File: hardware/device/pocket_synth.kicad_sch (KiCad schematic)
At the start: 0 parts

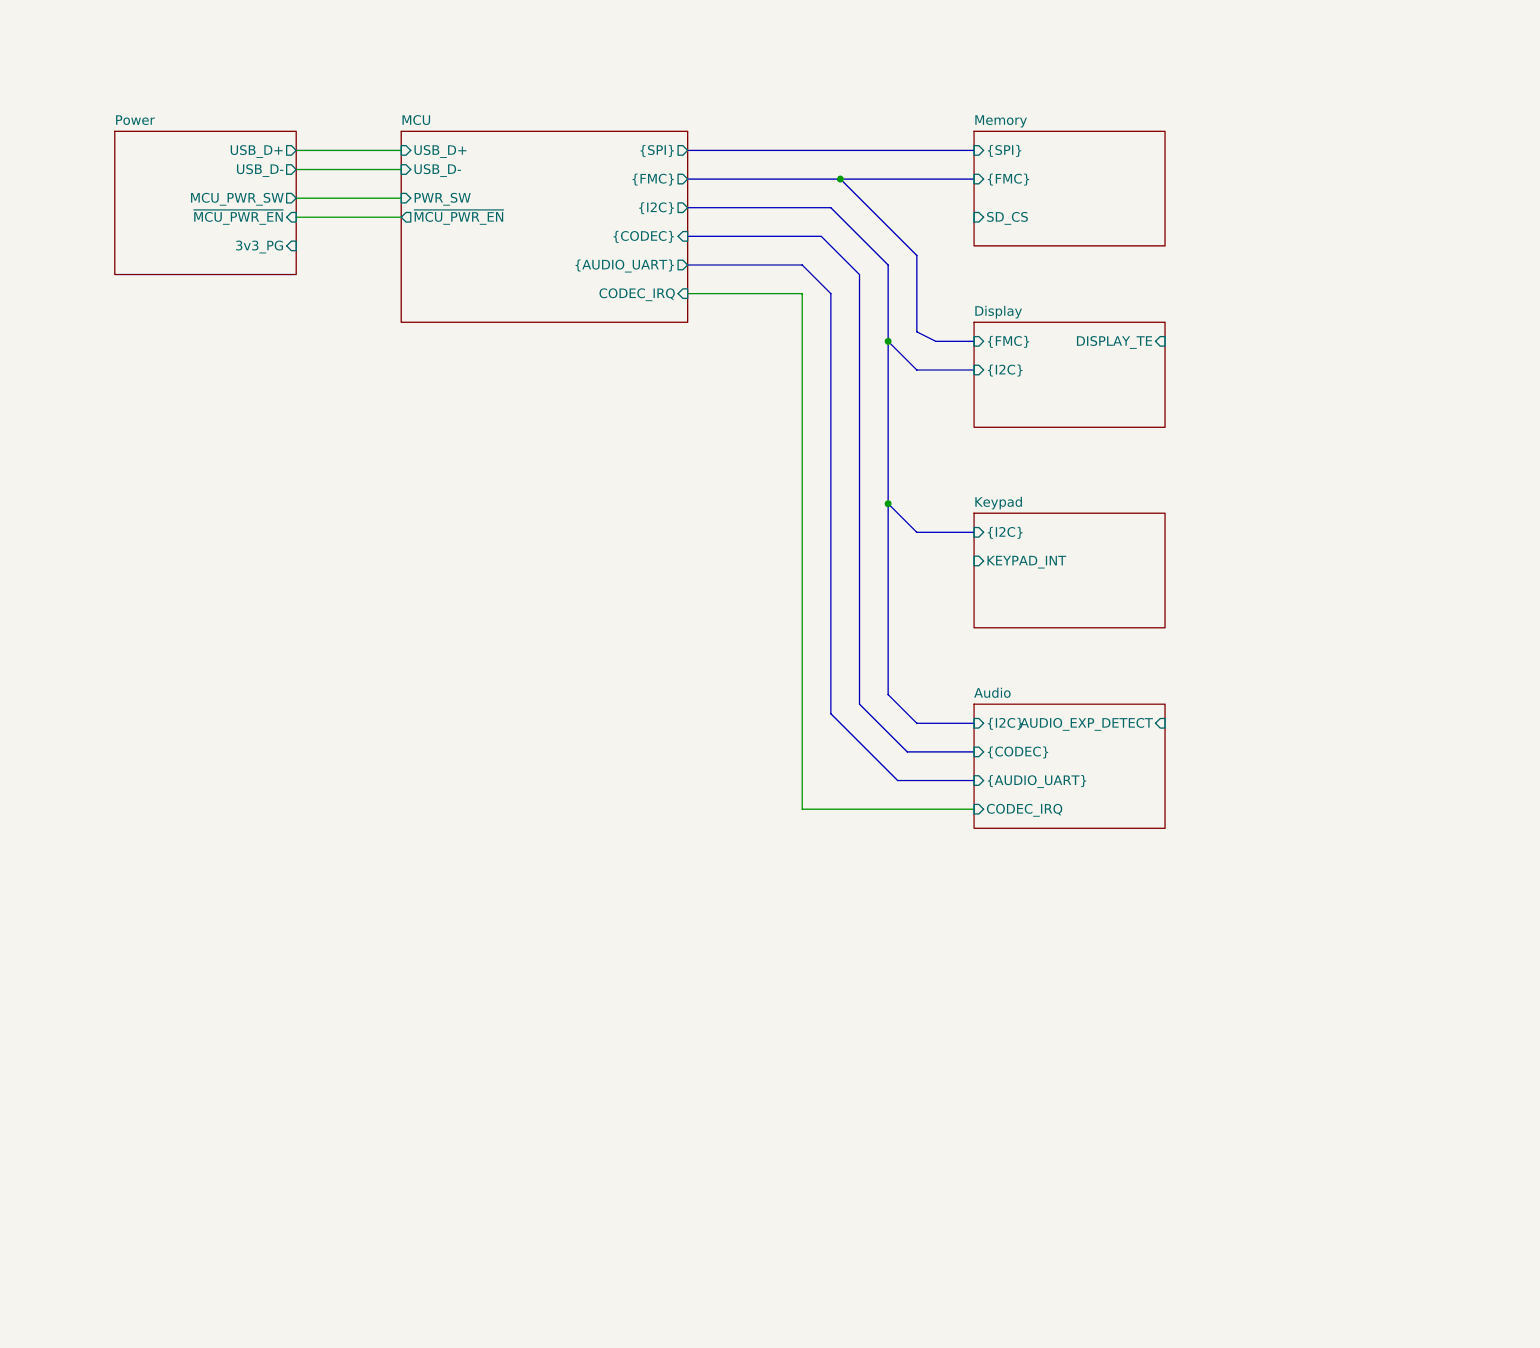
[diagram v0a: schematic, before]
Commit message: feat: various layout, start adding capacitive pads
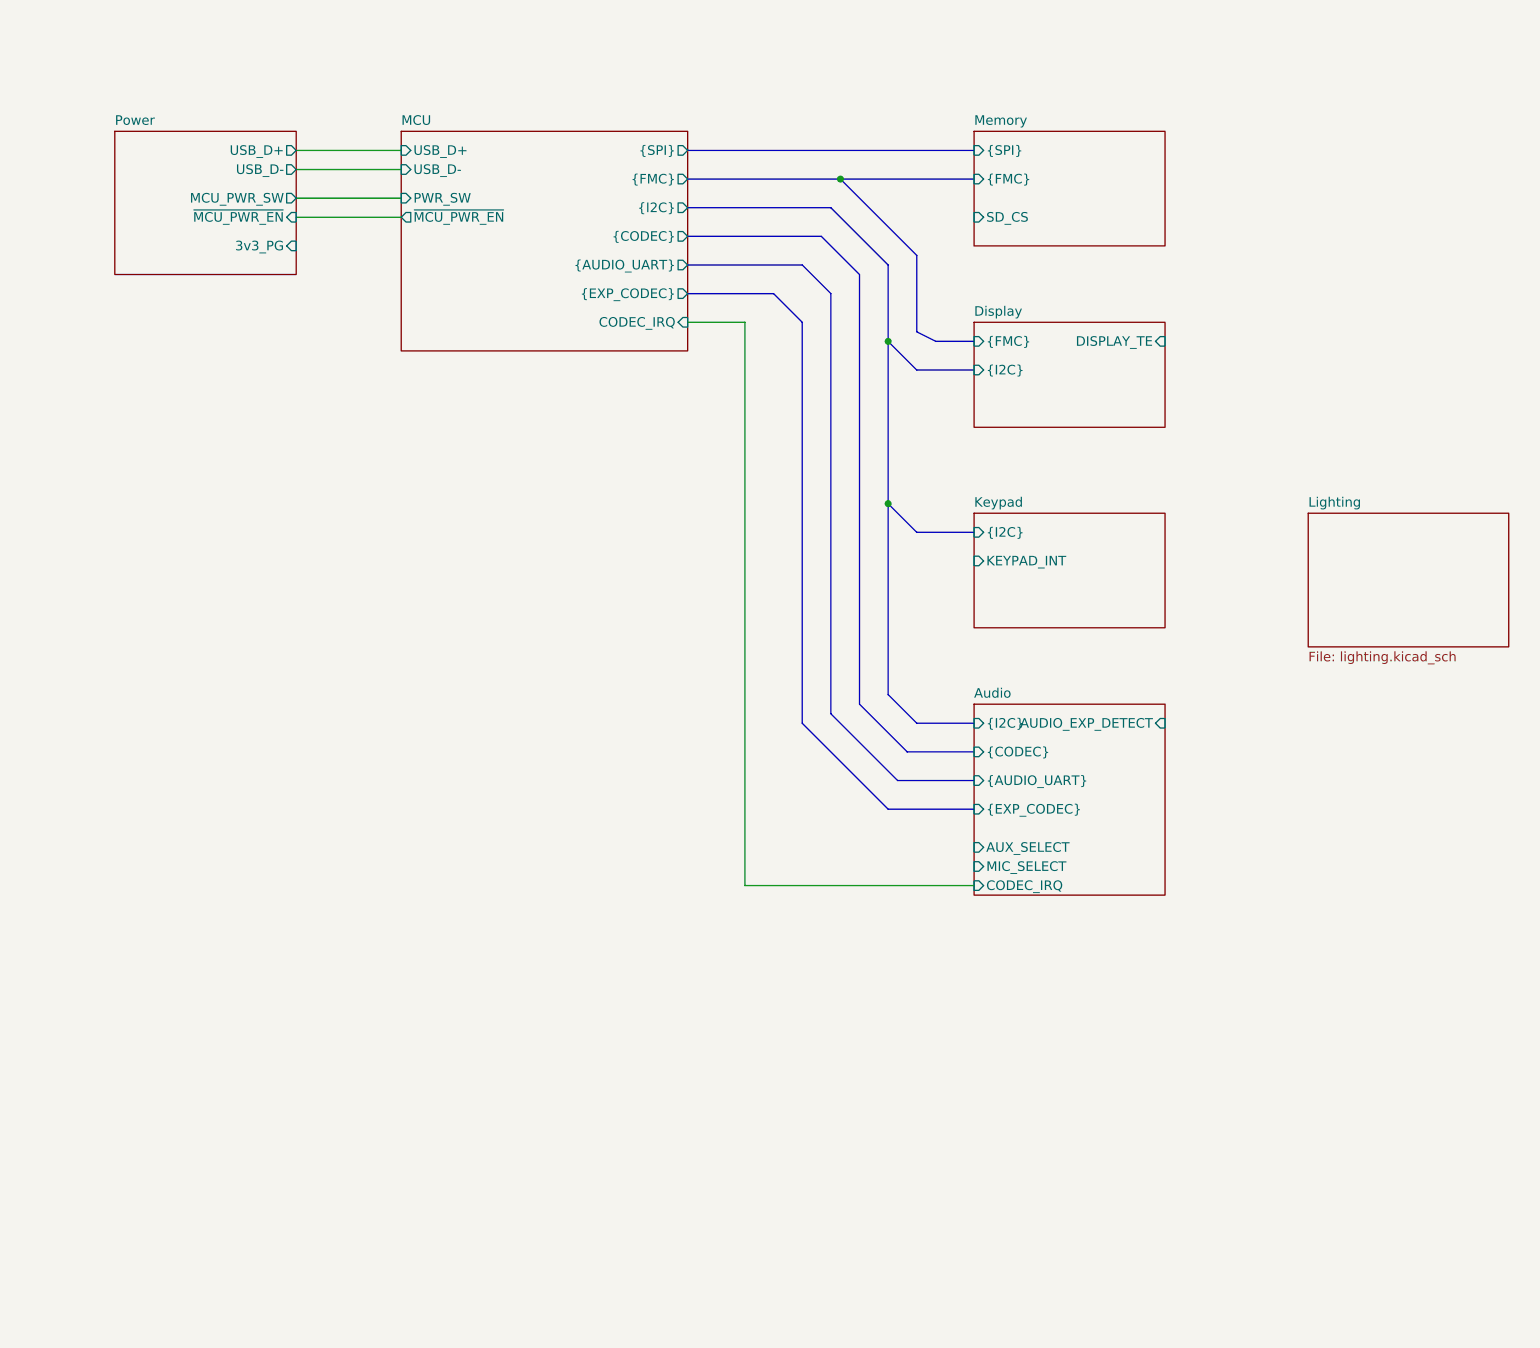
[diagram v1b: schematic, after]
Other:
- added sheet Lighting (lighting.kicad_sch)
- sheet Audio ports: added AUX_SELECT, MIC_SELECT, {EXP_CODEC}; removed none
- sheet MCU ports: added {EXP_CODEC}; removed none
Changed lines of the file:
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@@
 	(wire
 		(pts
-			(xy 116.84 59.69) (xy 116.84 128.27)
+			(xy 109.22 63.5) (xy 109.22 138.43)
+		)
+		(stroke
+			(width 0)
+			(type default)
+		)
+	)
+	(bus
+		(pts
+			(xy 113.03 59.69) (xy 116.84 63.5)
 		)
 		(stroke
@@
 	(wire
 		(pts
-			(xy 101.6 59.69) (xy 116.84 59.69)
+			(xy 101.6 63.5) (xy 109.22 63.5)
+		)
+		(stroke
+			(width 0)
+			(type default)
+		)
+	)
+	(bus
+		(pts
+			(xy 116.84 63.5) (xy 116.84 116.84)
 		)
 		(stroke
@@
 		)
 	)
+	(bus
+		(pts
+			(xy 101.6 59.69) (xy 113.03 59.69)
+		)
+		(stroke
+			(width 0)
+			(type default)
+		)
+	)
 	(wire
 		(pts
-			(xy 116.84 128.27) (xy 139.7 128.27)
+			(xy 109.22 138.43) (xy 139.7 138.43)
 		)
 		(stroke
@@
 	(bus
 		(pts
+			(xy 128.27 128.27) (xy 139.7 128.27)
+		)
+		(stroke
+			(width 0)
+			(type default)
+		)
+	)
+	(bus
+		(pts
 			(xy 120.65 115.57) (xy 129.54 124.46)
 		)
@@
 		(pts
 			(xy 101.6 44.45) (xy 121.92 44.45)
+		)
+		(stroke
+			(width 0)
+			(type default)
+		)
+	)
+	(bus
+		(pts
+			(xy 116.84 116.84) (xy 128.27 128.27)
 		)
 		(stroke
@@
 	(sheet
 		(at 63.5 38.1)
-		(size 38.1 25.4)
+		(size 38.1 29.21)
 		(exclude_from_sim no)
 		(in_bom yes)
@@
 		)
 		(property "Sheetfile" "MCU.kicad_sch"
-			(at 63.5 64.0846 0)
+			(at 63.5 67.8946 0)
 			(effects
 				(font
@@
 			)
 		)
-		(pin "{CODEC}" input
+		(pin "{CODEC}" output
 			(at 101.6 52.07 0)
 			(effects
@@
 		)
 		(pin "CODEC_IRQ" input
-			(at 101.6 59.69 0)
+			(at 101.6 63.5 0)
 			(effects
 				(font
@@
 		(pin "{AUDIO_UART}" output
 			(at 101.6 55.88 0)
+			(effects
+				(font
+					(size 1.27 1.27)
+				)
+				(justify right)
+			)
+		)
+		(pin "{EXP_CODEC}" output
+			(at 101.6 59.69 0)
 			(effects
 				(font
@@
 	(sheet
 		(at 139.7 114.3)
-		(size 25.4 16.51)
+		(size 25.4 25.4)
 		(exclude_from_sim no)
 		(in_bom yes)
@@
 		)
 		(property "Sheetfile" "audio.kicad_sch"
-			(at 139.7 131.3946 0)
+			(at 139.7 140.2846 0)
 			(effects
 				(font
@@
 		)
 		(pin "CODEC_IRQ" input
-			(at 139.7 128.27 180)
+			(at 139.7 138.43 180)
 			(effects
 				(font
@@
 		(pin "{AUDIO_UART}" input
 			(at 139.7 124.46 180)
+			(effects
+				(font
+					(size 1.27 1.27)
+				)
+				(justify left)
+			)
+		)
+		(pin "AUX_SELECT" input
+			(at 139.7 133.35 180)
+			(effects
+				(font
+					(size 1.27 1.27)
+				)
+				(justify left)
+			)
+		)
+		(pin "MIC_SELECT" input
+			(at 139.7 135.89 180)
+			(effects
+				(font
+					(size 1.27 1.27)
+				)
+				(justify left)
+			)
+		)
+		(pin "{EXP_CODEC}" input
+			(at 139.7 128.27 180)
 			(effects
 				(font
@@
 				)
 			)
+		)
+	)
+	(sheet
+		(at 184.15 88.9)
+		(size 26.67 17.78)
+		(exclude_from_sim no)
+		(in_bom yes)
+		(on_board yes)
+		(dnp no)
+		(fields_autoplaced yes)
+		(stroke
+			(width 0.1524)
+			(type solid)
+		)
+		(fill
+			(color 0 0 0 0.0000)
+		)
+		(property "Sheetname" "Lighting"
+			(at 184.15 88.1884 0)
+			(effects
+				(font
+					(size 1.27 1.27)
+				)
+				(justify left bottom)
+			)
+		)
+		(property "Sheetfile" "lighting.kicad_sch"
+			(at 184.15 107.2646 0)
+			(effects
+				(font
+					(size 1.27 1.27)
+				)
+				(justify left top)
+			)
+		)
+		(instances
+			(project "pocket_synth"
+				(path "/485383b8-00f4-4405-b270-de249939cff4"
+					(page "8")
+				)
+			)

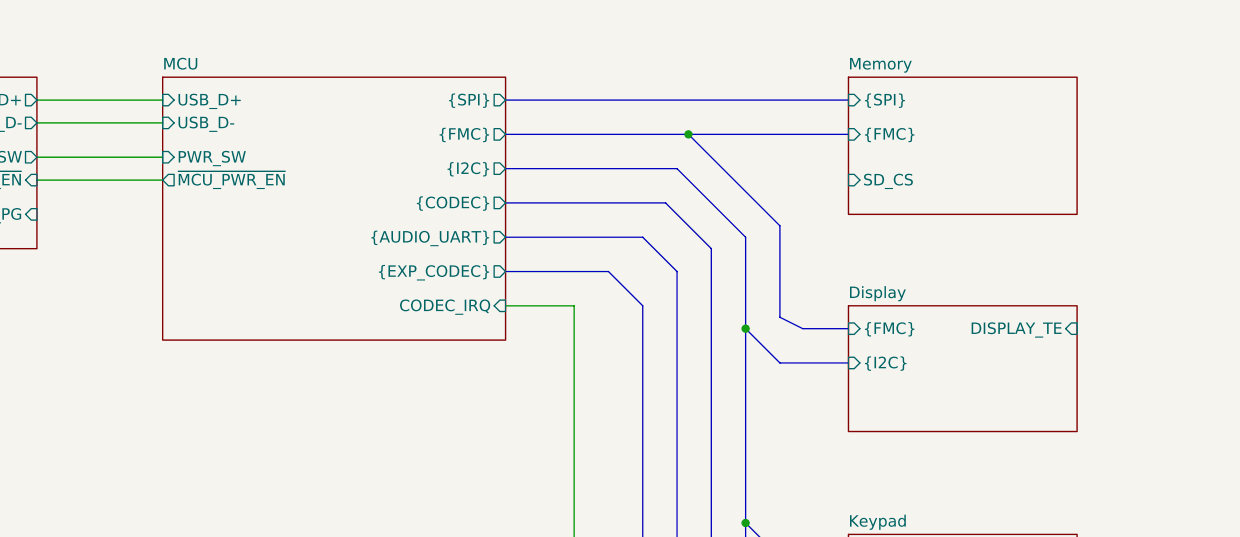
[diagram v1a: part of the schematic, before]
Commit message: feat: add integrated flash memory
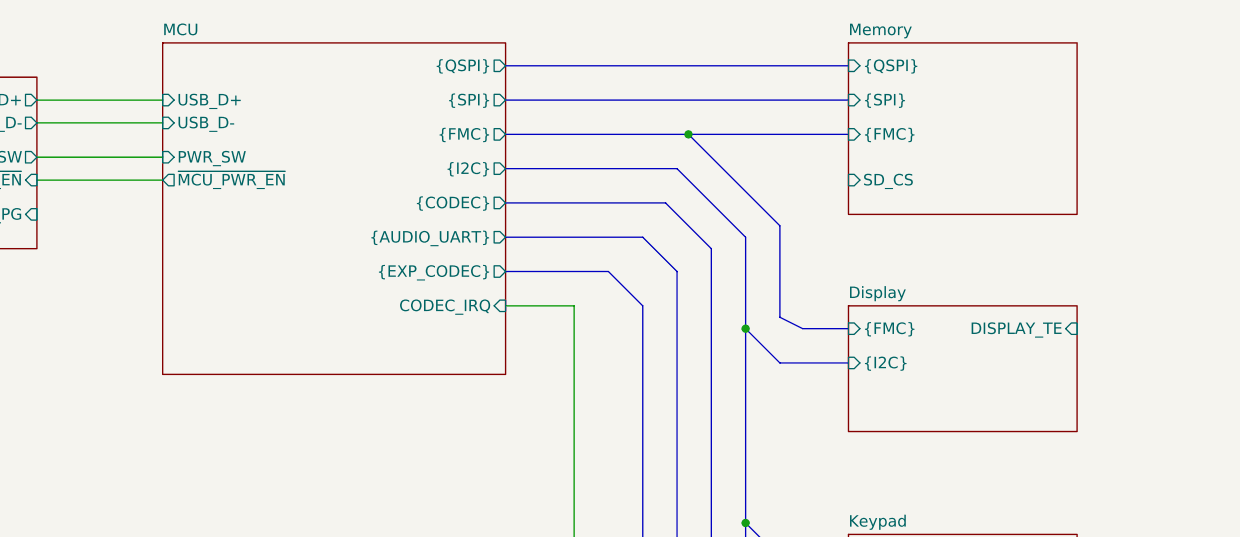
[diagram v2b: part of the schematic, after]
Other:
- sheet MCU ports: added {QSPI}; removed none
- sheet Memory ports: added {QSPI}; removed none
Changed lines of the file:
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@@
+	(bus
+		(pts
+			(xy 101.6 36.83) (xy 139.7 36.83)
+		)
+		(stroke
+			(width 0)
+			(type default)
+		)
+	)
 	(bus
 		(pts
@@
 	)
 	(sheet
-		(at 63.5 38.1)
-		(size 38.1 29.21)
+		(at 63.5 34.29)
+		(size 38.1 36.83)
 		(exclude_from_sim no)
 		(in_bom yes)
@@
 		)
 		(property "Sheetname" "MCU"
-			(at 63.5 37.3884 0)
+			(at 63.5 33.5784 0)
 			(effects
 				(font
@@
 		)
 		(property "Sheetfile" "MCU.kicad_sch"
-			(at 63.5 67.8946 0)
+			(at 63.5 71.7046 0)
 			(effects
 				(font
@@
 		(pin "{EXP_CODEC}" output
 			(at 101.6 59.69 0)
+			(effects
+				(font
+					(size 1.27 1.27)
+				)
+				(justify right)
+			)
+		)
+		(pin "{QSPI}" output
+			(at 101.6 36.83 0)
 			(effects
 				(font
@@
 	)
 	(sheet
-		(at 139.7 38.1)
-		(size 25.4 15.24)
+		(at 139.7 34.29)
+		(size 25.4 19.05)
 		(exclude_from_sim no)
 		(in_bom yes)
@@
 		)
 		(property "Sheetname" "Memory"
-			(at 139.7 37.3884 0)
+			(at 139.7 33.5784 0)
 			(effects
 				(font
@@
 			(effects
 				(font
+					(size 1.27 1.27)
+				)
+				(justify left)
+			)
+		)
+		(pin "{QSPI}" input
+			(at 139.7 36.83 180)
+			(effects
+				(font

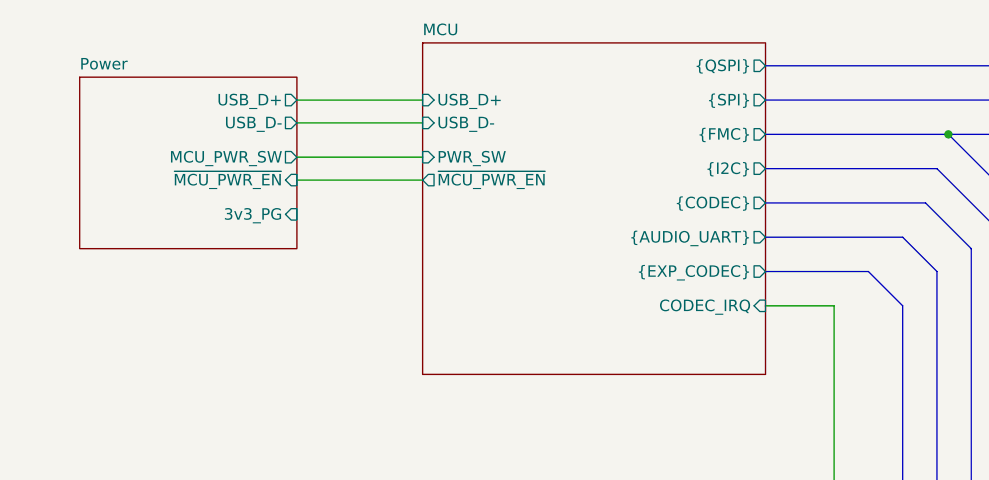
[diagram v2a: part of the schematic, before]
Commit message: feat: keypad schematic cleanup
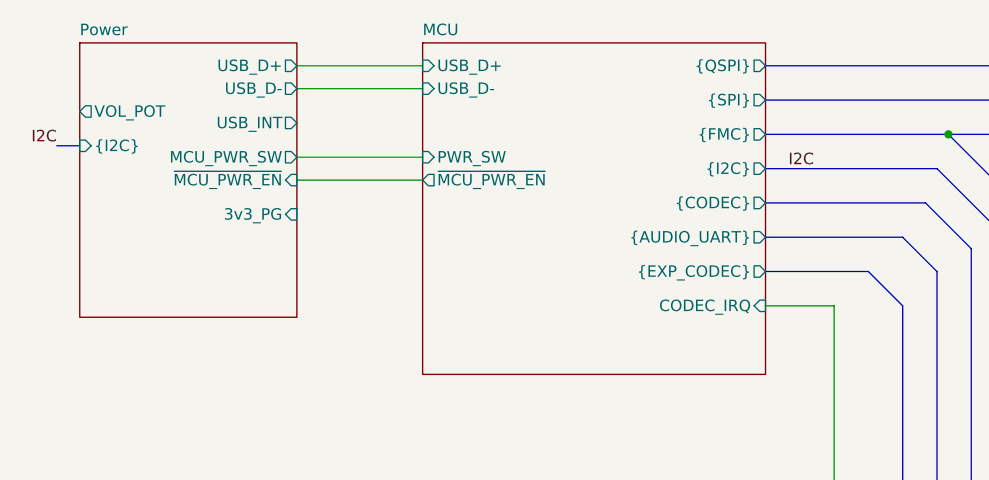
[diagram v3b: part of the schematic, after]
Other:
- sheet Power ports: added USB_INT, VOL_POT, {I2C}; removed none
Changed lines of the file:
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@@
 	(wire
 		(pts
-			(xy 49.53 43.18) (xy 63.5 43.18)
+			(xy 49.53 39.37) (xy 63.5 39.37)
 		)
 		(stroke
@@
 	(wire
 		(pts
-			(xy 49.53 40.64) (xy 63.5 40.64)
+			(xy 49.53 36.83) (xy 63.5 36.83)
 		)
 		(stroke
@@
 	(bus
 		(pts
+			(xy 22.86 45.72) (xy 25.4 45.72)
+		)
+		(stroke
+			(width 0)
+			(type default)
+		)
+	)
+	(bus
+		(pts
 			(xy 101.6 55.88) (xy 116.84 55.88)
 		)
@@
 			(width 0)
 			(type default)
+		)
+	)
+	(label "I2C"
+		(at 22.86 45.72 180)
+		(effects
+			(font
+				(size 1.27 1.27)
+				(thickness 0.1588)
+			)
+			(justify right bottom)
+		)
+	)
+	(label "I2C"
+		(at 104.14 48.26 0)
+		(effects
+			(font
+				(size 1.27 1.27)
+				(thickness 0.1588)
+			)
+			(justify left bottom)
 		)
 	)
@@
 		)
 		(pin "USB_D+" input
-			(at 63.5 40.64 180)
+			(at 63.5 36.83 180)
 			(effects
 				(font
@@
 		)
 		(pin "USB_D-" input
-			(at 63.5 43.18 180)
+			(at 63.5 39.37 180)
 			(effects
 				(font
@@
 	)
 	(sheet
-		(at 25.4 38.1)
-		(size 24.13 19.05)
+		(at 25.4 34.29)
+		(size 24.13 30.48)
 		(exclude_from_sim no)
 		(in_bom yes)
@@
 		)
 		(property "Sheetname" "Power"
-			(at 25.4 37.3884 0)
+			(at 25.4 33.5784 0)
 			(effects
 				(font
@@
 		)
 		(property "Sheetfile" "power.kicad_sch"
-			(at 25.4 57.7346 0)
+			(at 25.4 65.3546 0)
 			(effects
 				(font
@@
 		)
 		(pin "USB_D+" output
-			(at 49.53 40.64 0)
+			(at 49.53 36.83 0)
 			(effects
 				(font
@@
 		)
 		(pin "USB_D-" output
-			(at 49.53 43.18 0)
+			(at 49.53 39.37 0)
 			(effects
 				(font
@@
 			)
 		)
+		(pin "USB_INT" output
+			(at 49.53 43.18 0)
+			(effects
+				(font
+					(size 1.27 1.27)
+				)
+				(justify right)
+			)
+		)
+		(pin "VOL_POT" output
+			(at 25.4 41.91 180)
+			(effects
+				(font
+					(size 1.27 1.27)
+				)
+				(justify left)
+			)
+		)
+		(pin "{I2C}" input
+			(at 25.4 45.72 180)
+			(effects
+				(font
+					(size 1.27 1.27)
+				)
+				(justify left)
+			)
+		)
